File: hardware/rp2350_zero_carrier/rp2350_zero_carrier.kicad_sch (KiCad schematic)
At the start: 8 parts, among them J1 RP2350-Zero_Header(20pin,plac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, J2 USB-A_Host(VBUS/D-/D+/GND), SW1 SPST_Slide_Switch(Mute,SS-12S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, SW2 SPST_Slide_Switch(MirrorFilte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, SW3 SPST_Slide_Switch(Spare,SS-12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

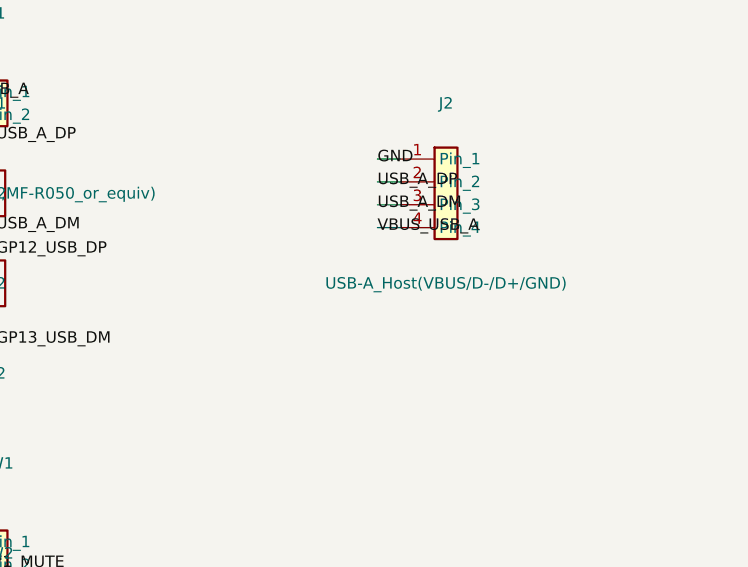
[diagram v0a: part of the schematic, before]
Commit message: J2(USB-A)にメーカー実図面ベースのカスタムfootprintを追加
オーケストレーターがNeltron 5075AR-04-WH(秋月100160)の実図面から取得した
寸法でfootprintを新規作成。信号ピン4本(⌀0.92mm丸穴、ピッチ2.50/2.00/2.50mm、
pin1=VBUS/2=D-/3=D+/4=GND)+シェル固定ペグ2本(⌀2.3mm NPTH、間隔13.14mm、
信号ピン列から2.70mmオフセット)。ローカルfootprintライブラリを解決するため
プロジェクト直下にfp-lib-tableを追加。

Co-Authored-By: Claude Sonnet 5 <noreply@anthropic.com>
Claude-Session: https://claude.ai/code/session_01E7QH5gCzZj3tVha83XRuUt
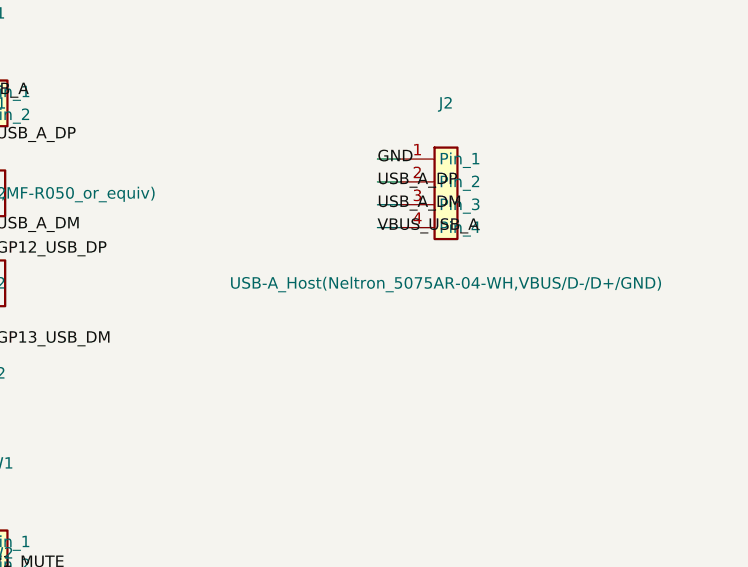
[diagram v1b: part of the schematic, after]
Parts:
- J2: value USB-A_Host(VBUS/D-/D+/GND) -> USB-A_Host(Neltron_5075AR-04-WH,VBUS/D-/D+/GND); footprint (none) -> rp2350_zero_carrier:USB_A_Neltron_5075AR-04-WH
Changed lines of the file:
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@@
     (in_bom yes) (on_board yes) (dnp no) (fields_autoplaced yes)
     (property "Reference" "J2" (at 160 80 0) (effects (font (size 1.27 1.27))))
-    (property "Value" "USB-A_Host(VBUS/D-/D+/GND)" (at 160 100 0) (effects (font (size 1.27 1.27))))
-    (property "Footprint" "" (at 160 90 0) (effects (font (size 1.27 1.27)) hide))
+    (property "Value" "USB-A_Host(Neltron_5075AR-04-WH,VBUS/D-/D+/GND)" (at 160 100 0) (effects (font (size 1.27 1.27))))
+    (property "Footprint" "rp2350_zero_carrier:USB_A_Neltron_5075AR-04-WH" (at 160 90 0) (effects (font (size 1.27 1.27)) hide))
     (property "Datasheet" "" (at 160 90 0) (effects (font (size 1.27 1.27)) hide))
     (pin "1")

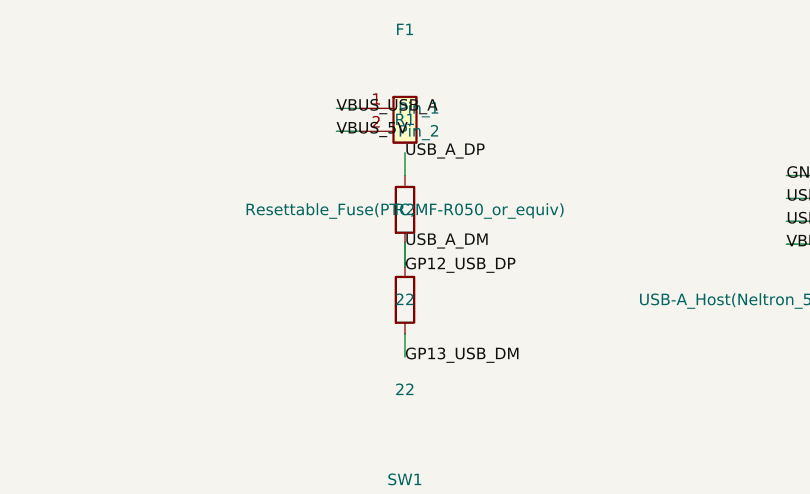
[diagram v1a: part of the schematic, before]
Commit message: F1(リセッタブルヒューズ)にBourns MF-R050の実データシートベースfootprintを追加
型番を秋月112628(Bourns MF-R050)で確定(前回の「MF-R050相当」から訂正)。
リード径0.51mm・ピッチ5.1mm(公称)のラジアルリード品として、ドリル0.8mm
丸穴×2のカスタムfootprintを作成。

Co-Authored-By: Claude Sonnet 5 <noreply@anthropic.com>
Claude-Session: https://claude.ai/code/session_01E7QH5gCzZj3tVha83XRuUt
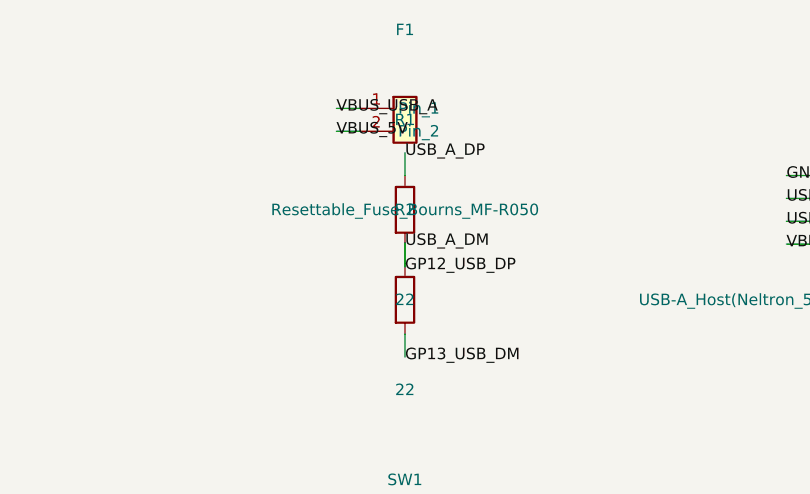
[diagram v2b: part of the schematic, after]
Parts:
- F1: value Resettable_Fuse(PTC,MF-R050_or_equiv) -> Resettable_Fuse_Bourns_MF-R050; footprint (none) -> rp2350_zero_carrier:Fuse_Bourns_MF-R050_Radial
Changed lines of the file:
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@@
     (in_bom yes) (on_board yes) (dnp no) (fields_autoplaced yes)
     (property "Reference" "F1" (at 110 70 0) (effects (font (size 1.27 1.27))))
-    (property "Value" "Resettable_Fuse(PTC,MF-R050_or_equiv)" (at 110 90 0) (effects (font (size 1.27 1.27))))
-    (property "Footprint" "" (at 110 80 0) (effects (font (size 1.27 1.27)) hide))
+    (property "Value" "Resettable_Fuse_Bourns_MF-R050" (at 110 90 0) (effects (font (size 1.27 1.27))))
+    (property "Footprint" "rp2350_zero_carrier:Fuse_Bourns_MF-R050_Radial" (at 110 80 0) (effects (font (size 1.27 1.27)) hide))
     (property "Datasheet" "" (at 110 80 0) (effects (font (size 1.27 1.27)) hide))
     (pin "1")

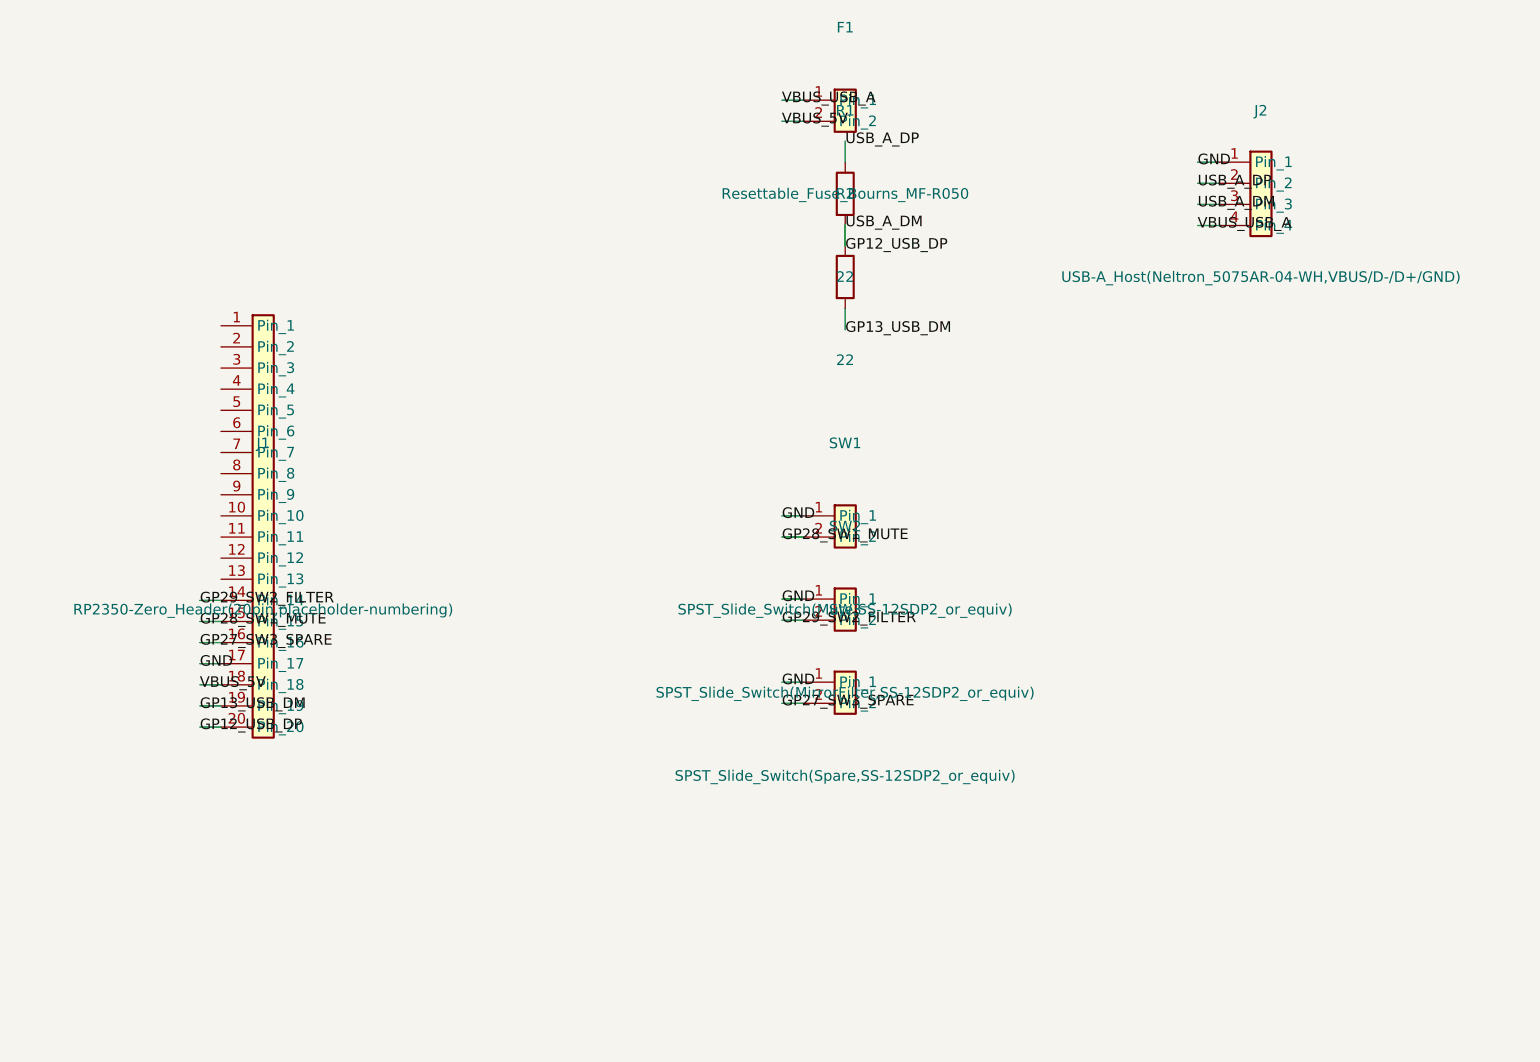
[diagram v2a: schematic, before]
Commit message: スイッチをSPST前提から3pin(1回路2接点/SPDT)ON-OFF配線に訂正
秋月電子には基板用SPST(2pin)スライドスイッチが無く、市販は1回路2接点(SPDT,
3pin)品のみと判明したため訂正。中央コモンをGPIOへ、片側接点をGNDへ、残り
1接点はNCとするON-OFF配線に変更。回路図もSwitch:SW_SPDTシンボル(3pin)へ
差し替え、NKK 115643(通販コード115643)の実図面(端子断面0.6x0.4mm平角、
2.54mmピッチ)に基づく角形パッドのfootprintを新規作成。

SW1-3は元のConn_01x02より縦に大きいシンボルになったため、相互干渉を避ける
ためY方向の配置間隔を10mm→25mmに広げた(SW2: y140→155, SW3: y150→180)。

Co-Authored-By: Claude Sonnet 5 <noreply@anthropic.com>
Claude-Session: https://claude.ai/code/session_01E7QH5gCzZj3tVha83XRuUt
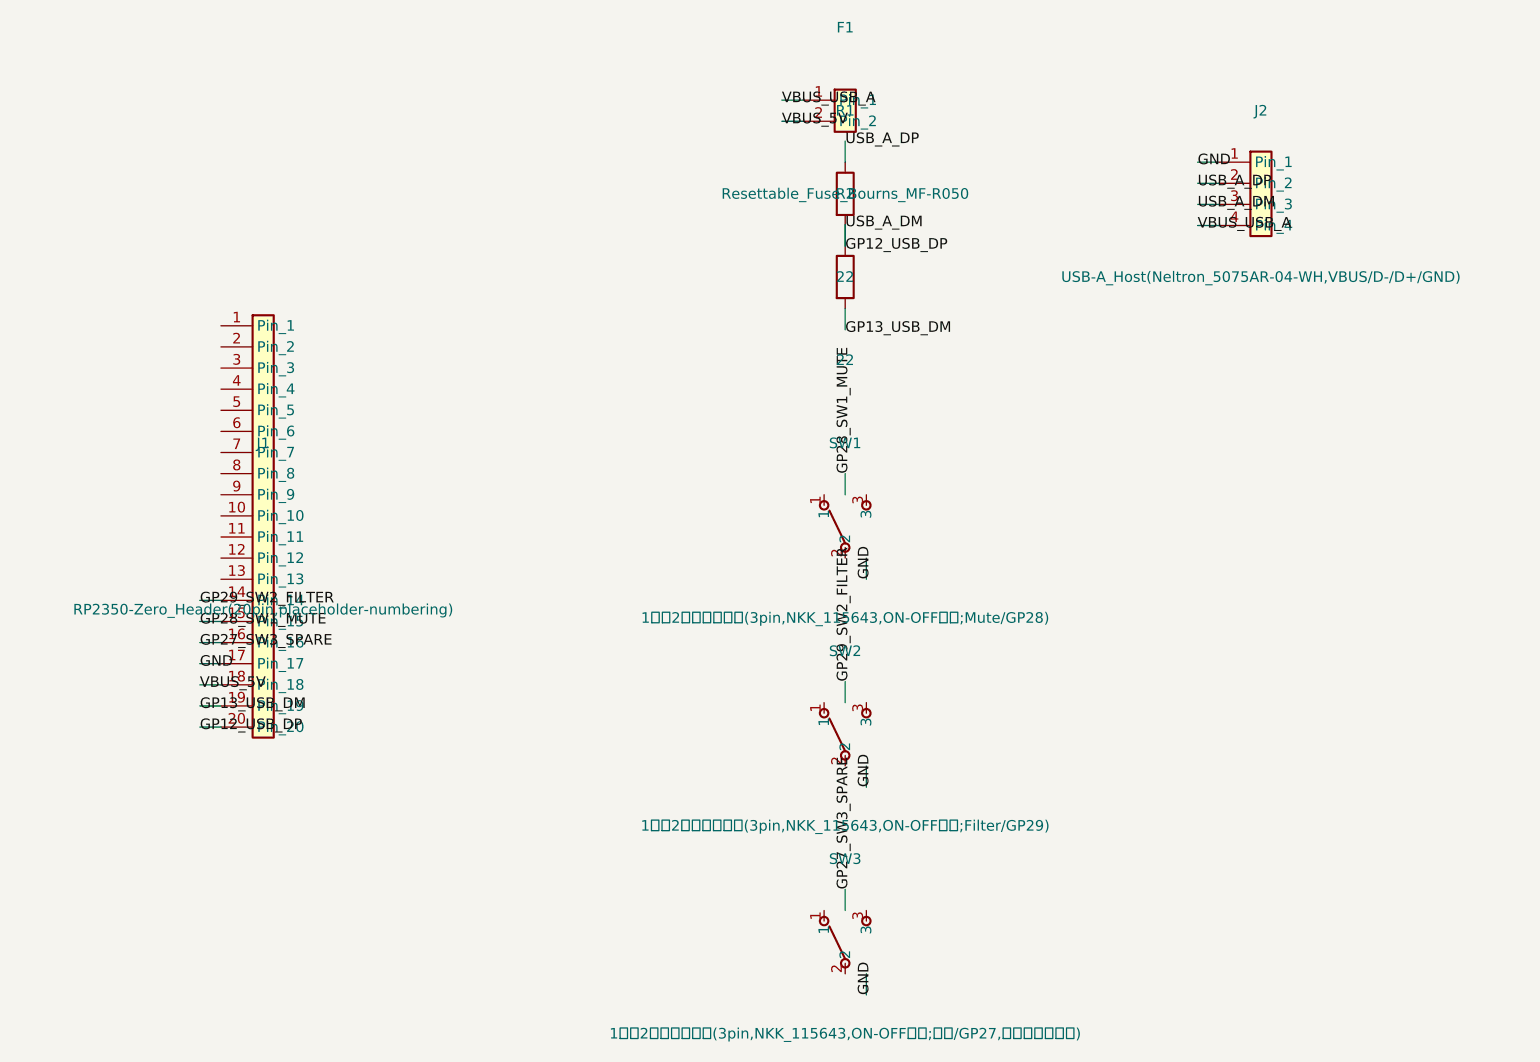
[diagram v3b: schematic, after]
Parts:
- SW1: value SPST_Slide_Switch(Mute,SS-12SDP2_or_equiv) -> 1回路2接点スイッチ(3pin,NKK_115643,ON-OFF用途;Mute/GP28); footprint (none) -> rp2350_zero_carrier:SW_SPDT_NKK_115643_Slide; symbol Connector_Generic:Conn_01x02 -> Switch:SW_SPDT
- SW2: value SPST_Slide_Switch(MirrorFilter,SS-12SDP2_or_equiv) -> 1回路2接点スイッチ(3pin,NKK_115643,ON-OFF用途;Filter/GP29); footprint (none) -> rp2350_zero_carrier:SW_SPDT_NKK_115643_Slide; symbol Connector_Generic:Conn_01x02 -> Switch:SW_SPDT
- SW3: value SPST_Slide_Switch(Spare,SS-12SDP2_or_equiv) -> 1回路2接点スイッチ(3pin,NKK_115643,ON-OFF用途;予備/GP27,ファーム未対応); footprint (none) -> rp2350_zero_carrier:SW_SPDT_NKK_115643_Slide; symbol Connector_Generic:Conn_01x02 -> Switch:SW_SPDT
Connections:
- net GND: no longer SW1.1 (Pin_1), SW2.1 (Pin_1), SW3.1 (Pin_1)
- net GP27_SW3_SPARE: no longer SW3.2 (Pin_2)
- net GP28_SW1_MUTE: no longer SW1.2 (Pin_2)
- net GP29_SW2_FILTER: no longer SW2.2 (Pin_2)
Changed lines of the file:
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@@
     )
   )
-  (symbol (lib_id "Connector_Generic:Conn_01x02") (at 110 130 0) (unit 1)
+  (symbol (lib_id "Switch:SW_SPDT") (at 110 130 0) (unit 1)
     (in_bom yes) (on_board yes) (dnp no) (fields_autoplaced yes)
     (property "Reference" "SW1" (at 110 120 0) (effects (font (size 1.27 1.27))))
-    (property "Value" "SPST_Slide_Switch(Mute,SS-12SDP2_or_equiv)" (at 110 140 0) (effects (font (size 1.27 1.27))))
-    (property "Footprint" "" (at 110 130 0) (effects (font (size 1.27 1.27)) hide))
+    (property "Value" "1回路2接点スイッチ(3pin,NKK_115643,ON-OFF用途;Mute/GP28)" (at 110 141 0) (effects (font (size 1.27 1.27))))
+    (property "Footprint" "rp2350_zero_carrier:SW_SPDT_NKK_115643_Slide" (at 110 130 0) (effects (font (size 1.27 1.27)) hide))
     (property "Datasheet" "" (at 110 130 0) (effects (font (size 1.27 1.27)) hide))
     (pin "1")
     (pin "2")
+    (pin "3")
     (instances
       (project "rp2350_zero_carrier"
@@
     )
   )
-  (symbol (lib_id "Connector_Generic:Conn_01x02") (at 110 140 0) (unit 1)
+  (symbol (lib_id "Switch:SW_SPDT") (at 110 155 0) (unit 1)
     (in_bom yes) (on_board yes) (dnp no) (fields_autoplaced yes)
-    (property "Reference" "SW2" (at 110 130 0) (effects (font (size 1.27 1.27))))
-    (property "Value" "SPST_Slide_Switch(MirrorFilter,SS-12SDP2_or_equiv)" (at 110 150 0) (effects (font (size 1.27 1.27))))
-    (property "Footprint" "" (at 110 140 0) (effects (font (size 1.27 1.27)) hide))
-    (property "Datasheet" "" (at 110 140 0) (effects (font (size 1.27 1.27)) hide))
+    (property "Reference" "SW2" (at 110 145 0) (effects (font (size 1.27 1.27))))
+    (property "Value" "1回路2接点スイッチ(3pin,NKK_115643,ON-OFF用途;Filter/GP29)" (at 110 166 0) (effects (font (size 1.27 1.27))))
+    (property "Footprint" "rp2350_zero_carrier:SW_SPDT_NKK_115643_Slide" (at 110 155 0) (effects (font (size 1.27 1.27)) hide))
+    (property "Datasheet" "" (at 110 155 0) (effects (font (size 1.27 1.27)) hide))
     (pin "1")
     (pin "2")
+    (pin "3")
     (instances
       (project "rp2350_zero_carrier"
@@
     )
   )
-  (symbol (lib_id "Connector_Generic:Conn_01x02") (at 110 150 0) (unit 1)
+  (symbol (lib_id "Switch:SW_SPDT") (at 110 180 0) (unit 1)
     (in_bom yes) (on_board yes) (dnp no) (fields_autoplaced yes)
-    (property "Reference" "SW3" (at 110 140 0) (effects (font (size 1.27 1.27))))
-    (property "Value" "SPST_Slide_Switch(Spare,SS-12SDP2_or_equiv)" (at 110 160 0) (effects (font (size 1.27 1.27))))
-    (property "Footprint" "" (at 110 150 0) (effects (font (size 1.27 1.27)) hide))
-    (property "Datasheet" "" (at 110 150 0) (effects (font (size 1.27 1.27)) hide))
+    (property "Reference" "SW3" (at 110 170 0) (effects (font (size 1.27 1.27))))
+    (property "Value" "1回路2接点スイッチ(3pin,NKK_115643,ON-OFF用途;予備/GP27,ファーム未対応)" (at 110 191 0) (effects (font (size 1.27 1.27))))
+    (property "Footprint" "rp2350_zero_carrier:SW_SPDT_NKK_115643_Slide" (at 110 180 0) (effects (font (size 1.27 1.27)) hide))
+    (property "Datasheet" "" (at 110 180 0) (effects (font (size 1.27 1.27)) hide))
     (pin "1")
     (pin "2")
+    (pin "3")
     (instances
       (project "rp2350_zero_carrier"
@@
   (wire (pts (xy 154.92 88.73) (xy 152.38 88.73)) (stroke (width 0) (type default)))
   (wire (pts (xy 154.92 86.19) (xy 152.38 86.19)) (stroke (width 0) (type default)))
-  (wire (pts (xy 104.92 131.27) (xy 102.38 131.27)) (stroke (width 0) (type default)))
-  (wire (pts (xy 104.92 128.73) (xy 102.38 128.73)) (stroke (width 0) (type default)))
-  (wire (pts (xy 104.92 141.27) (xy 102.38 141.27)) (stroke (width 0) (type default)))
-  (wire (pts (xy 104.92 138.73) (xy 102.38 138.73)) (stroke (width 0) (type default)))
-  (wire (pts (xy 104.92 151.27) (xy 102.38 151.27)) (stroke (width 0) (type default)))
-  (wire (pts (xy 104.92 148.73) (xy 102.38 148.73)) (stroke (width 0) (type default)))
+  (wire (pts (xy 110 126.19) (xy 110 123.65)) (stroke (width 0) (type default)))
+  (wire (pts (xy 112.54 133.81) (xy 112.54 136.35)) (stroke (width 0) (type default)))
+  (wire (pts (xy 110 151.19) (xy 110 148.65)) (stroke (width 0) (type default)))
+  (wire (pts (xy 112.54 158.81) (xy 112.54 161.35)) (stroke (width 0) (type default)))
+  (wire (pts (xy 110 176.19) (xy 110 173.65)) (stroke (width 0) (type default)))
+  (wire (pts (xy 112.54 183.81) (xy 112.54 186.35)) (stroke (width 0) (type default)))
   (label "GP12_USB_DP" (at 32.38 154.13 0) (effects (font (size 1.27 1.27)) (justify left)))
   (label "GP13_USB_DM" (at 32.38 151.59 0) (effects (font (size 1.27 1.27)) (justify left)))
@@
   (label "USB_A_DP" (at 152.38 88.73 0) (effects (font (size 1.27 1.27)) (justify left)))
   (label "GND" (at 152.38 86.19 0) (effects (font (size 1.27 1.27)) (justify left)))
-  (label "GP28_SW1_MUTE" (at 102.38 131.27 0) (effects (font (size 1.27 1.27)) (justify left)))
-  (label "GND" (at 102.38 128.73 0) (effects (font (size 1.27 1.27)) (justify left)))
-  (label "GP29_SW2_FILTER" (at 102.38 141.27 0) (effects (font (size 1.27 1.27)) (justify left)))
-  (label "GND" (at 102.38 138.73 0) (effects (font (size 1.27 1.27)) (justify left)))
-  (label "GP27_SW3_SPARE" (at 102.38 151.27 0) (effects (font (size 1.27 1.27)) (justify left)))
-  (label "GND" (at 102.38 148.73 0) (effects (font (size 1.27 1.27)) (justify left)))
+  (label "GP28_SW1_MUTE" (at 110 123.65 90) (effects (font (size 1.27 1.27)) (justify left)))
+  (label "GND" (at 112.54 136.35 90) (effects (font (size 1.27 1.27)) (justify left)))
+  (label "GP29_SW2_FILTER" (at 110 148.65 90) (effects (font (size 1.27 1.27)) (justify left)))
+  (label "GND" (at 112.54 161.35 90) (effects (font (size 1.27 1.27)) (justify left)))
+  (label "GP27_SW3_SPARE" (at 110 173.65 90) (effects (font (size 1.27 1.27)) (justify left)))
+  (label "GND" (at 112.54 186.35 90) (effects (font (size 1.27 1.27)) (justify left)))
   (sheet_instances
     (path "/" (page "1"))
